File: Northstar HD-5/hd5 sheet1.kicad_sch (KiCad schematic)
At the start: 39 parts, among them Q1 2N3904, U1B 26LS31, U1C 74S10, U1D 74S00, U1E 50ns_Delay, U1F 74S04, U1K LM393, U1L 7438, U1M 74LS374, U2D 74LS175, U2E 82S129, U2F 74S174, U2J 74LS393, U2K 74LS393, U2L 2114, U2M 2114, U3K 74LS164, U3L 74LS374, U3M 74LS166, U4J 74LS04, U4K 74LS244, U4L 74LS244, U4M 74LS244, U5L 74LS138, U5M 74LS138

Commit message: changes to hd-5 and gitignore
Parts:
- C12: footprint (none) -> Capacitor_THT:C_Disc_D10.0mm_W2.5mm_P5.00mm
- C3, C4: footprint (none) -> Capacitor_THT:C_Rect_L10.0mm_W5.0mm_P5.00mm_P7.50mm
- C9: footprint (none) -> Capacitor_THT:CP_Radial_Tantal_D5.0mm_P2.50mm
- CR3: footprint Diode_THT:D_DO-35_SOD27_P7.62mm_Horizontal -> Diode_THT:D_A-405_P12.70mm_Horizontal
- Q1: footprint Package_TO_SOT_THT:TO-92_Inline -> Package_TO_SOT_THT:TO-92L_Wide
- R23, R26, R27, R5, R6: footprint (none) -> Resistor_THT:R_Axial_DIN0309_L9.0mm_D3.2mm_P12.70mm_Horizontal
- R24, R25: footprint (none) -> Resistor_THT:R_Axial_DIN0207_L6.3mm_D2.5mm_P15.24mm_Horizontal
- TP2: footprint Connector_Pin:Pin_D1.0mm_L10.0mm -> Connector_PinHeader_2.54mm:PinHeader_1x01_P2.54mm_Vertical
- U1B1: renamed from U1B; footprint (none) -> Package_DIP:DIP-16_W7.62mm
- U1C1: renamed from U1C; footprint (none) -> Package_DIP:DIP-14_W7.62mm
- U1D1: renamed from U1D; footprint (none) -> Package_DIP:DIP-14_W7.62mm
- U1E1: renamed from U1E; footprint (none) -> Package_DIP:DIP-14_W7.62mm
- U1F1: renamed from U1F; footprint (none) -> Package_DIP:DIP-14_W7.62mm
- U1K1: renamed from U1K; footprint (none) -> Package_DIP:DIP-8-16_W7.62mm
- U1L1: renamed from U1L; footprint (none) -> Package_DIP:DIP-14_W7.62mm
- U1M1: renamed from U1M; footprint (none) -> Package_DIP:DIP-20_W7.62mm
- U2D1: renamed from U2D; footprint (none) -> Package_DIP:DIP-16_W7.62mm
- U2E1: renamed from U2E; footprint (none) -> Package_DIP:DIP-16_W7.62mm
- U2F1: renamed from U2F; footprint (none) -> Package_DIP:DIP-16_W7.62mm
- U2J1: renamed from U2J; footprint (none) -> Package_DIP:DIP-14_W7.62mm
- U2K1: renamed from U2K; footprint (none) -> Package_DIP:DIP-14_W7.62mm
- U2L1: renamed from U2L; footprint (none) -> Package_DIP:DIP-18_W7.62mm
- U2M1: renamed from U2M; footprint (none) -> Package_DIP:DIP-18_W7.62mm
- U3K1: renamed from U3K; footprint DIP794W53P254L1930H508Q14N -> Package_DIP:DIP-14_W7.62mm
- U3L1: renamed from U3L; footprint (none) -> Package_DIP:DIP-20_W7.62mm
- U3M1: renamed from U3M; footprint (none) -> Package_DIP:DIP-16_W7.62mm
- U4J1: renamed from U4J; footprint (none) -> Package_DIP:DIP-14_W7.62mm
- U4K1: renamed from U4K; footprint (none) -> Package_DIP:DIP-20_W7.62mm
- U4L1: renamed from U4L; footprint (none) -> Package_DIP:DIP-20_W7.62mm
- U4M1: renamed from U4M; footprint (none) -> Package_DIP:DIP-20_W7.62mm
- U5L1: renamed from U5L; footprint (none) -> Package_DIP:DIP-16_W7.62mm
- U5M1: renamed from U5M; footprint (none) -> Package_DIP:DIP-16_W7.62mm
- XTL1: footprint (none) -> Crystal:Crystal_HC49-U_Horizontal

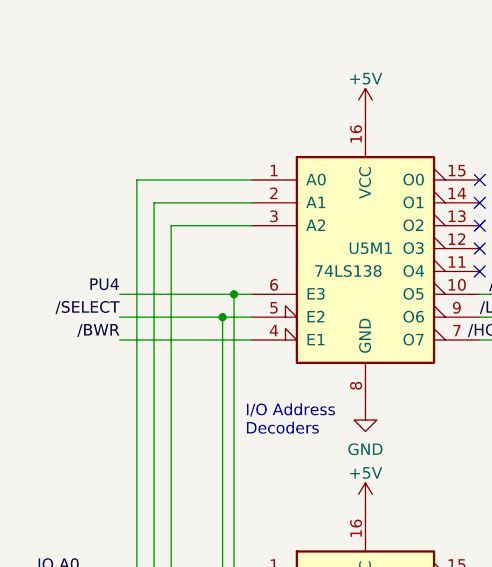
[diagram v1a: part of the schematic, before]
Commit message: placed components for column 5
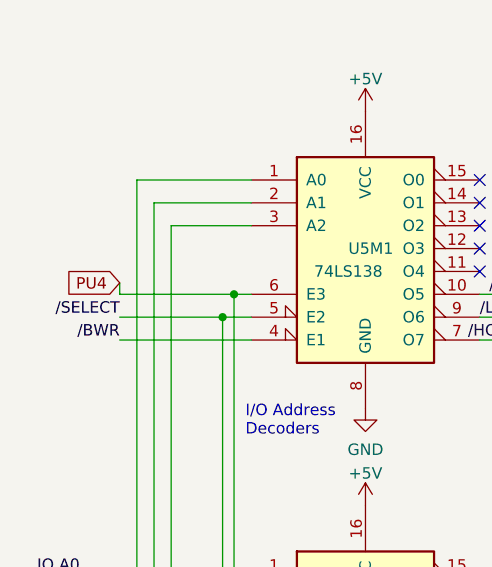
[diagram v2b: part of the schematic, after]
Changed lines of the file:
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@@
+    (stroke (width 0) (type default) (color 0 0 0 0))
+  )
+  (wire (pts (xy 56.515 92.71) (xy 56.515 93.98))
     (stroke (width 0) (type default) (color 0 0 0 0))
   )
@@
     (effects (font (size 1.27 1.27)) (justify left bottom))
   )
-  (label "PU4" (at 56.515 93.98 180)
-    (effects (font (size 1.27 1.27)) (justify right bottom))
-  )
   (label "HD2" (at 142.24 47.625 0)
     (effects (font (size 1.27 1.27)) (justify left bottom))
@@
     (effects (font (size 1.27 1.27)) (justify left bottom))
   )
+  (global_label "PU4" (shape input) (at 56.515 92.71 180) (fields_autoplaced)
+    (effects (font (size 1.27 1.27)) (justify right))
+    (property "Intersheet References" "${INTERSHEET_REFS}" (id 0) (at 50.2919 92.7894 0)
+      (effects (font (size 1.27 1.27)) (justify right) hide)
+    )
+  )
   (symbol (lib_id "power:+5V") (at 226.695 112.395 0) (unit 1)

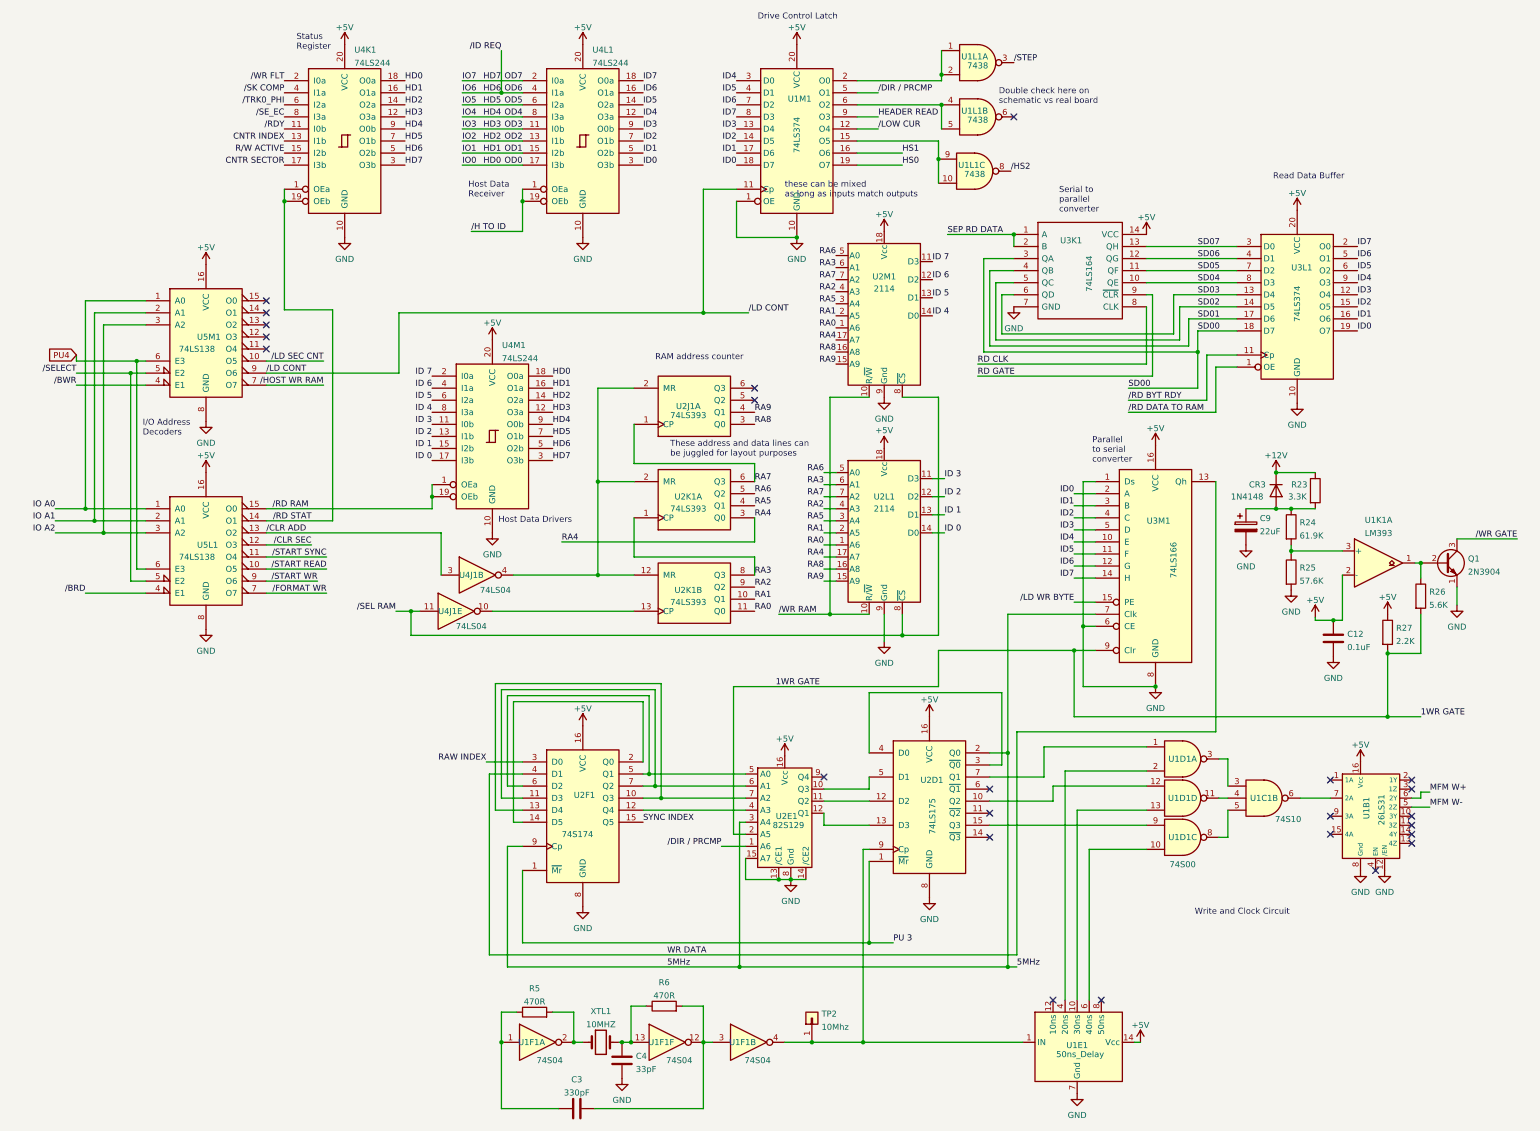
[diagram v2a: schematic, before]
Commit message: placed components and repaired multi sheet labels
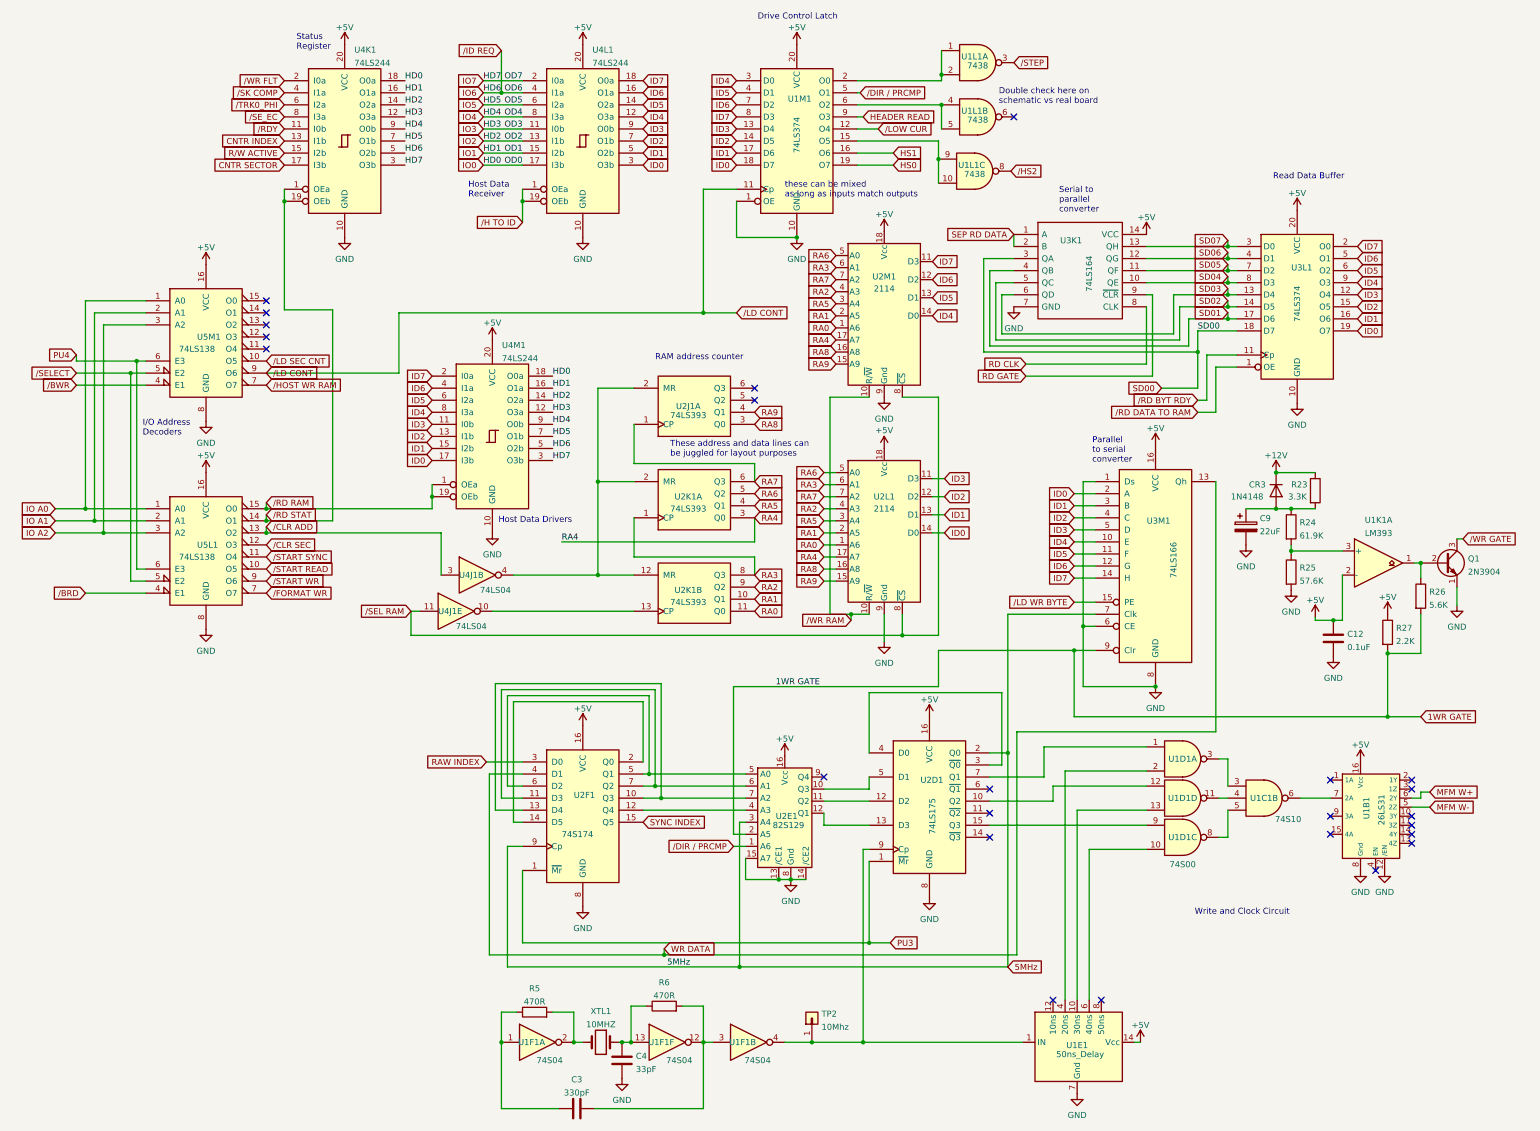
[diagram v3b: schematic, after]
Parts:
- U1K1: footprint Package_DIP:DIP-8-16_W7.62mm -> Package_DIP:DIP-8_W7.62mm
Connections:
- net ID 0 is gone; now on net ID0: U2L1.14 (D0), U4M1.17 (I3b)
- net ID 1 is gone; now on net ID1: U2L1.13 (D1), U4M1.15 (I2b)
- net ID 2 is gone; now on net ID2: U2L1.12 (D2), U4M1.13 (I1b)
- net ID 3 is gone; now on net ID3: U2L1.11 (D3), U4M1.11 (I0b)
- net ID 4 is gone; now on net ID4: U2M1.14 (D0), U4M1.8 (I3a)
- net ID 5 is gone; now on net ID5: U2M1.13 (D1), U4M1.6 (I2a)
- net ID 6 is gone; now on net ID6: U2M1.12 (D2), U4M1.4 (I1a)
- net ID 7 is gone; now on net ID7: U2M1.11 (D3), U4M1.2 (I0a)
- net at C4.1, R6.1, U1F1.13: now also XTL1.1; no longer XTL1.2
- net at R5.2, U1F1.2: now also XTL1.2; no longer XTL1.1
- net HD0 renamed IO0
- net HD1 renamed IO1
- net HD2 renamed IO2
- net HD3 renamed IO3
- net HD4 renamed IO4
- net HD5 renamed IO5
- net HD6 renamed IO6
- net HD7 renamed IO7
- net PU 3 renamed PU3

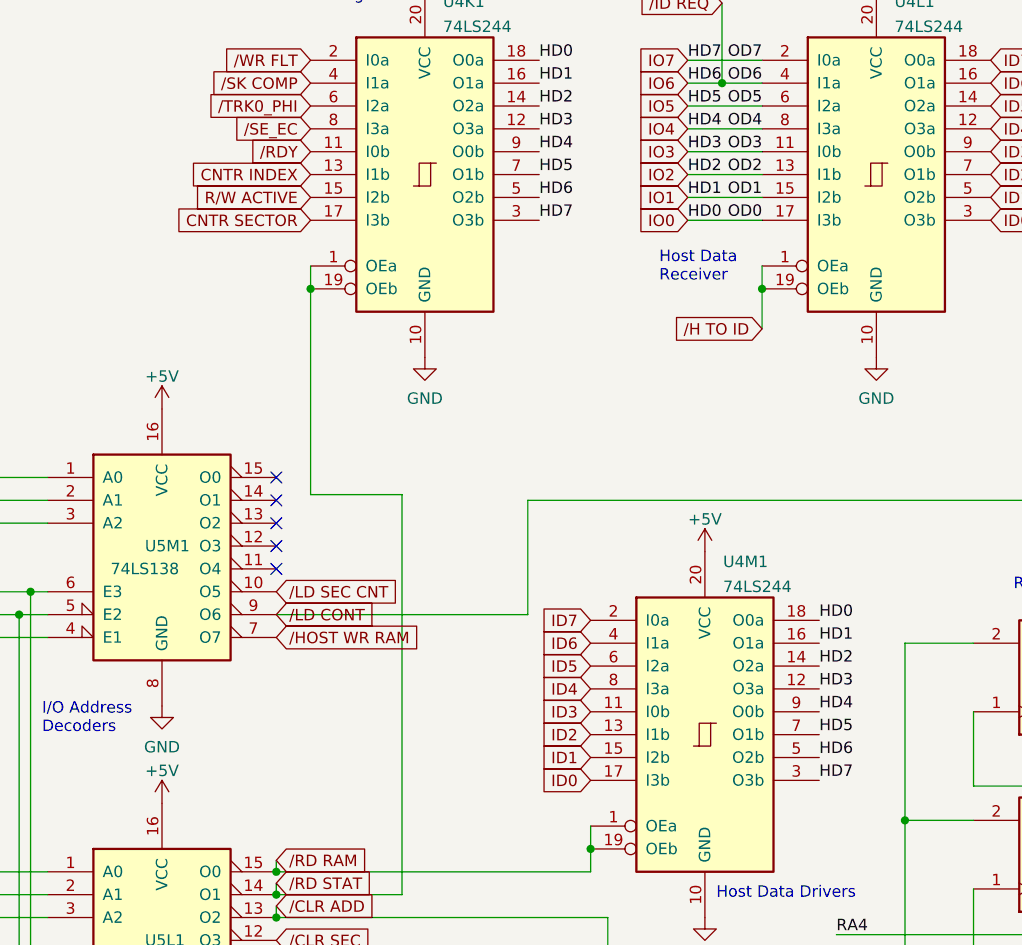
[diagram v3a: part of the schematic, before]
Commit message: finished signal routing top and bottom (assumed correct)
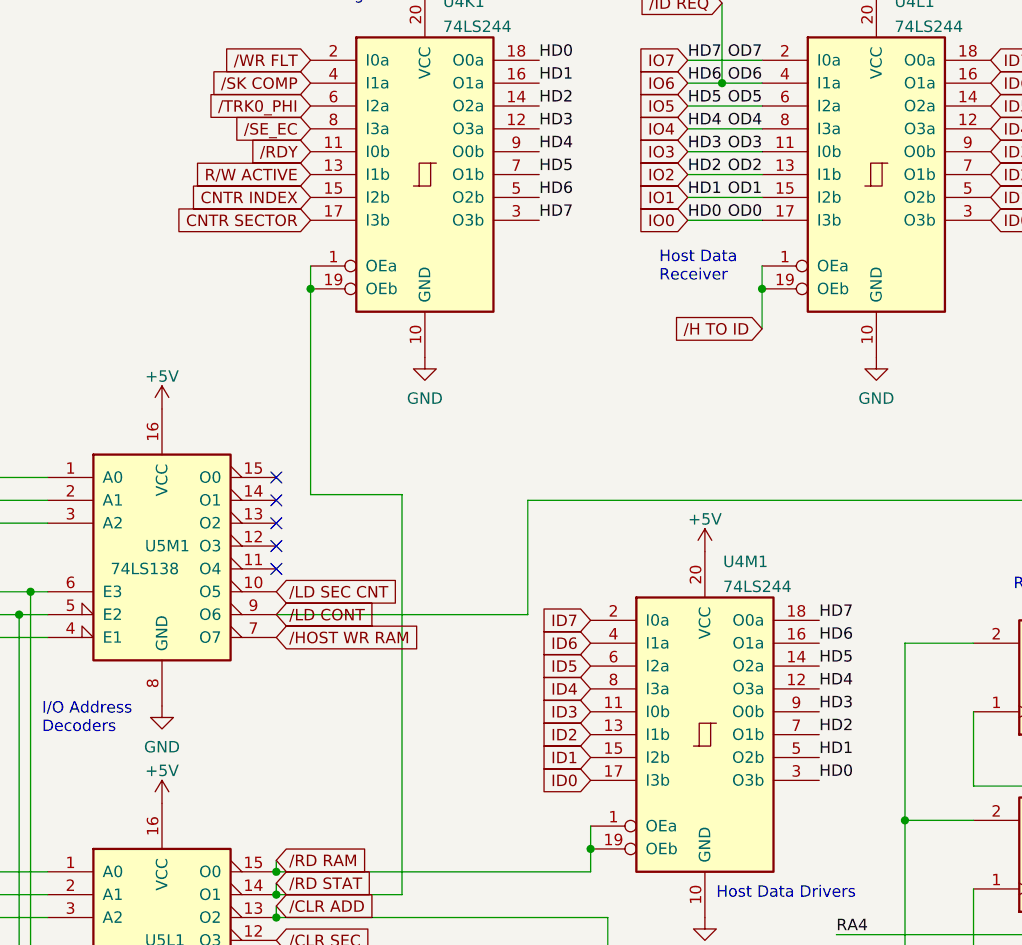
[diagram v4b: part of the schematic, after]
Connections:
- net CNTR INDEX: now also U4K1.15 (I2b); no longer U4K1.13 (I1b)
- net IO0: now also U4M1.3 (O3b); no longer U4M1.18 (O0a)
- net IO1: now also U4M1.5 (O2b); no longer U4M1.16 (O1a)
- net IO2: now also U4M1.7 (O1b); no longer U4M1.14 (O2a)
- net IO3: now also U4M1.9 (O0b); no longer U4M1.12 (O3a)
- net IO4: now also U4M1.12 (O3a); no longer U4M1.9 (O0b)
- net IO5: now also U4M1.14 (O2a); no longer U4M1.7 (O1b)
- net IO6: now also U4M1.16 (O1a); no longer U4M1.5 (O2b)
- net IO7: now also U4M1.18 (O0a); no longer U4M1.3 (O3b)
- net R/W ACTIVE: now also U4K1.13 (I1b); no longer U4K1.15 (I2b)
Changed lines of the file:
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@@
-    (effects (font (size 1.27 1.27)) (justify left bottom))
-  )
-  (label "HD1" (at 156.845 99.695 0)
-    (effects (font (size 1.27 1.27)) (justify left bottom))
-  )
-  (label "HD5" (at 156.845 109.855 0)
     (effects (font (size 1.27 1.27)) (justify left bottom))
   )
@@
     (effects (font (size 1.27 1.27)) (justify left bottom))
   )
-  (label "HD2" (at 156.845 102.235 0)
+  (label "HD2" (at 156.845 109.855 0)
+    (effects (font (size 1.27 1.27)) (justify left bottom))
+  )
+  (label "HD3" (at 156.845 107.315 0)
     (effects (font (size 1.27 1.27)) (justify left bottom))
   )
@@
     (effects (font (size 1.27 1.27)) (justify left bottom))
   )
-  (label "HD6" (at 156.845 112.395 0)
-    (effects (font (size 1.27 1.27)) (justify left bottom))
-  )
   (label "SD00" (at 292.735 87.63 0)
     (effects (font (size 1.27 1.27)) (justify left bottom))
@@
     (effects (font (size 1.27 1.27)) (justify left bottom))
   )
+  (label "HD4" (at 156.845 104.775 0)
+    (effects (font (size 1.27 1.27)) (justify left bottom))
+  )
   (label "HD6" (at 142.24 37.465 0)
     (effects (font (size 1.27 1.27)) (justify left bottom))
   )
-  (label "HD4" (at 156.845 107.315 0)
-    (effects (font (size 1.27 1.27)) (justify left bottom))
-  )
   (label "OD2" (at 146.685 47.625 0)
     (effects (font (size 1.27 1.27)) (justify left bottom))
@@
     (effects (font (size 1.27 1.27)) (justify left bottom))
   )
+  (label "HD7" (at 156.845 97.155 0)
+    (effects (font (size 1.27 1.27)) (justify left bottom))
+  )
   (label "HD6" (at 125.73 50.165 0)
     (effects (font (size 1.27 1.27)) (justify left bottom))
@@
     (effects (font (size 1.27 1.27)) (justify left bottom))
   )
+  (label "HD5" (at 156.845 102.235 0)
+    (effects (font (size 1.27 1.27)) (justify left bottom))
+  )
   (label "HD4" (at 125.73 45.085 0)
     (effects (font (size 1.27 1.27)) (justify left bottom))
   )
-  (label "HD3" (at 156.845 104.775 0)
+  (label "HD0" (at 156.845 114.935 0)
     (effects (font (size 1.27 1.27)) (justify left bottom))
   )
@@
     (effects (font (size 1.27 1.27)) (justify left bottom))
   )
-  (label "HD7" (at 156.845 114.935 0)
-    (effects (font (size 1.27 1.27)) (justify left bottom))
-  )
   (label "OD7" (at 146.685 34.925 0)
     (effects (font (size 1.27 1.27)) (justify left bottom))
@@
     (effects (font (size 1.27 1.27)) (justify left bottom))
   )
-  (label "HD0" (at 156.845 97.155 0)
+  (label "HD1" (at 156.845 112.395 0)
+    (effects (font (size 1.27 1.27)) (justify left bottom))
+  )
+  (label "HD6" (at 156.845 99.695 0)
     (effects (font (size 1.27 1.27)) (justify left bottom))
   )
@@
     )
   )
-  (global_label "CNTR INDEX" (shape input) (at 100.33 47.625 180) (fields_autoplaced)
-    (effects (font (size 1.27 1.27)) (justify right))
-    (property "Intersheet References" "${INTERSHEET_REFS}" (id 0) (at 86.5474 47.7044 0)
-      (effects (font (size 1.27 1.27)) (justify right) hide)
-    )
-  )
   (global_label "{slash}RD RAM" (shape input) (at 96.52 123.825 0) (fields_autoplaced)
     (effects (font (size 1.27 1.27)) (justify left))
@@
     )
   )
-  (global_label "R{slash}W ACTIVE" (shape input) (at 100.33 50.165 180) (fields_autoplaced)
-    (effects (font (size 1.27 1.27)) (justify right))
-    (property "Intersheet References" "${INTERSHEET_REFS}" (id 0) (at 86.7288 50.2444 0)
-      (effects (font (size 1.27 1.27)) (justify right) hide)
-    )
-  )
   (global_label "RA9" (shape input) (at 213.995 140.335 180) (fields_autoplaced)
     (effects (font (size 1.27 1.27)) (justify right))
@@
     )
   )
+  (global_label "R{slash}W ACTIVE" (shape input) (at 100.33 47.625 180) (fields_autoplaced)
+    (effects (font (size 1.27 1.27)) (justify right))
+    (property "Intersheet References" "${INTERSHEET_REFS}" (id 0) (at 86.7288 47.7044 0)
+      (effects (font (size 1.27 1.27)) (justify right) hide)
+    )
+  )
   (global_label "RA7" (shape input) (at 199.39 119.38 0) (fields_autoplaced)
     (effects (font (size 1.27 1.27)) (justify left))
@@
     )
   )
+  (global_label "CNTR INDEX" (shape input) (at 100.33 50.165 180) (fields_autoplaced)
+    (effects (font (size 1.27 1.27)) (justify right))
+    (property "Intersheet References" "${INTERSHEET_REFS}" (id 0) (at 86.5474 50.2444 0)
+      (effects (font (size 1.27 1.27)) (justify right) hide)
+    )
+  )
